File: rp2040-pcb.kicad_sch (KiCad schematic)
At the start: 43 parts, among them J1 Conn_01x20_Male, J2 Conn_01x20_Male, J3 105450-0101, SW1 SW_Push, SW2 SW_Push, U1 TPS54202DDC, U2 W25Q128JVSIQ, U3 RP2040, Y1 12 MHz

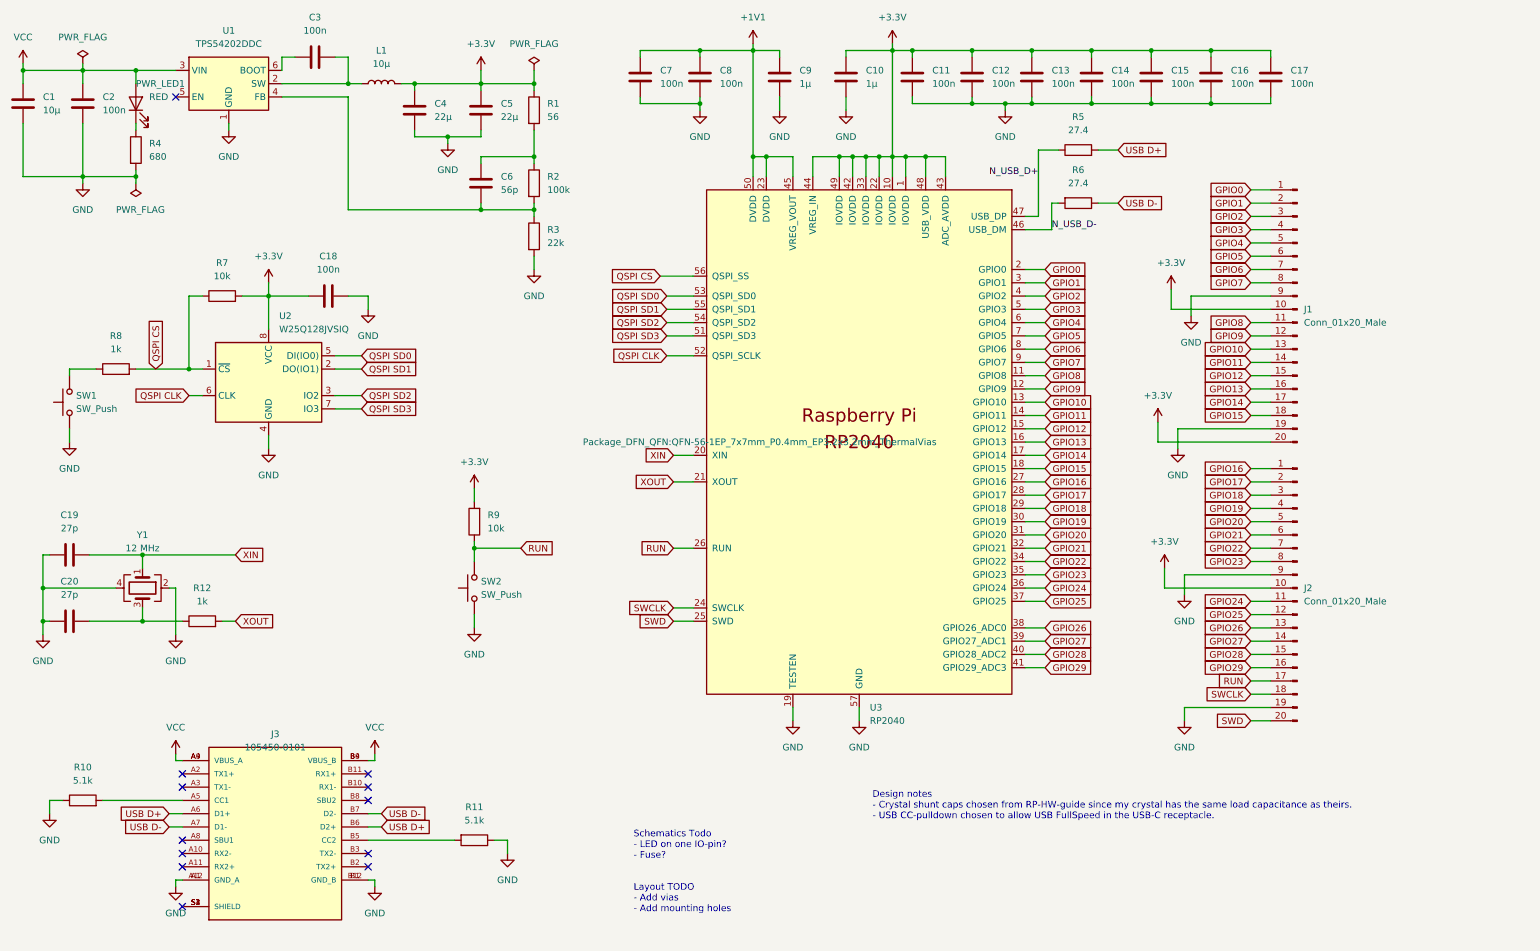
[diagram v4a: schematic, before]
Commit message: Updated numbering. Updated USB footpring on PCB.
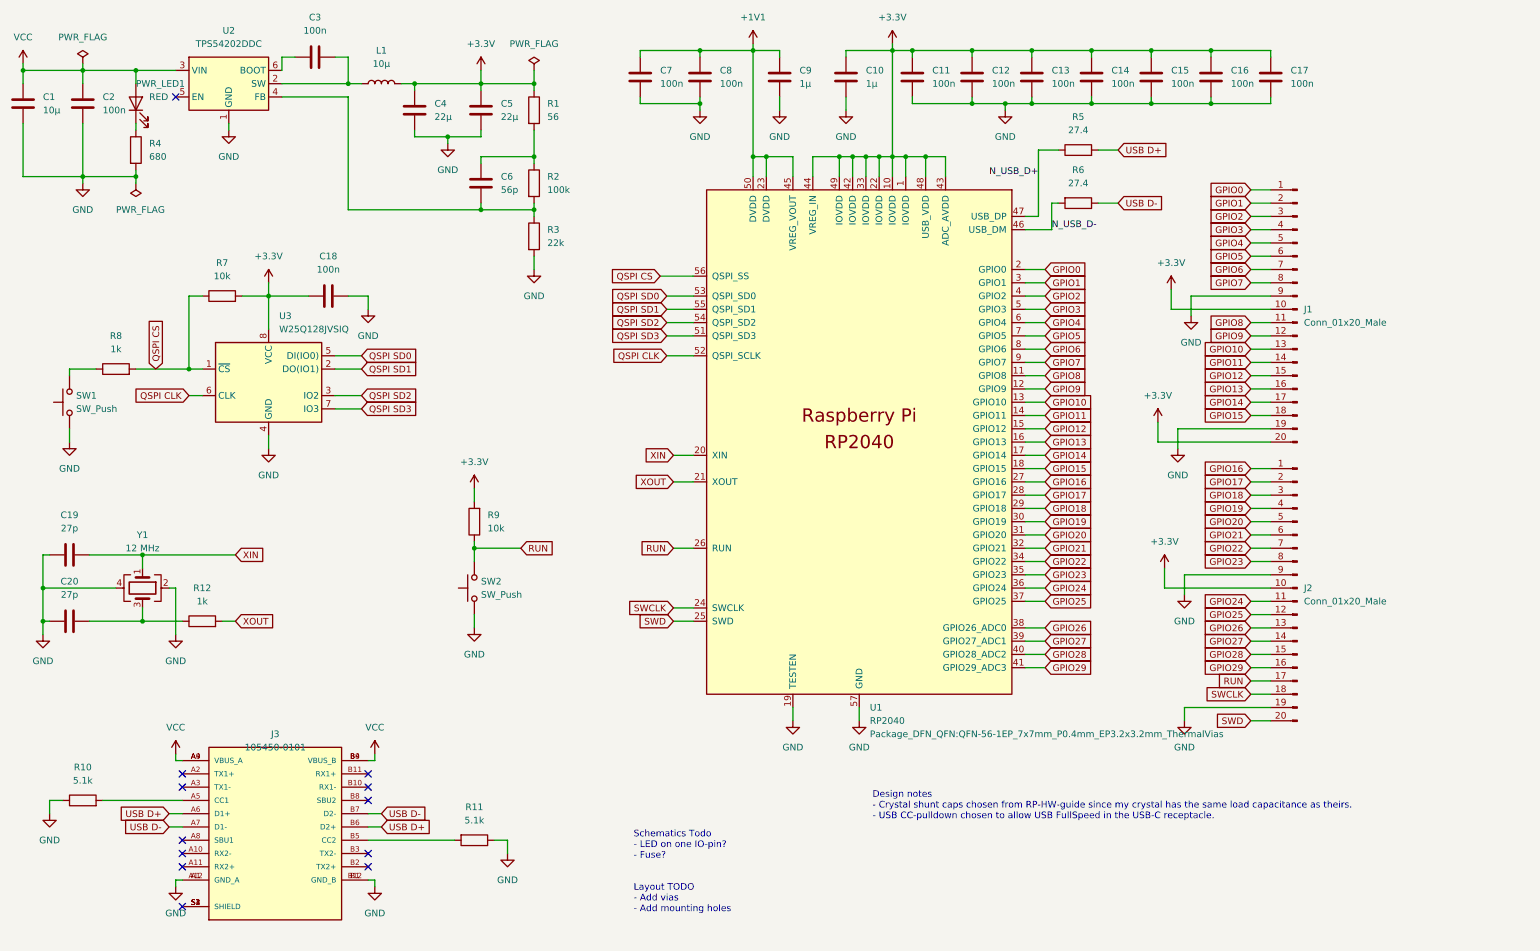
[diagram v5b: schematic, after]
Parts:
- renumbered U3 to U1, U1 to U2, U2 to U3
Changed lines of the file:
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@@
   (symbol (lib_id "MCU_RaspberryPi_RP2040:RP2040") (at 176.53 101.6 0) (unit 1)
     (in_bom yes) (on_board yes) (fields_autoplaced)
-    (property "Reference" "U3" (id 0) (at 178.5494 152.4 0)
+    (property "Reference" "U1" (id 0) (at 178.5494 152.4 0)
       (effects (font (size 1.27 1.27)) (justify left))
     )
@@
       (effects (font (size 1.27 1.27)) (justify left))
     )
-    (property "Footprint" "Package_DFN_QFN:QFN-56-1EP_7x7mm_P0.4mm_EP3.2x3.2mm_ThermalVias" (id 2) (at 157.48 101.6 0))
+    (property "Footprint" "Package_DFN_QFN:QFN-56-1EP_7x7mm_P0.4mm_EP3.2x3.2mm_ThermalVias" (id 2) (at 178.5494 157.48 0)
+      (effects (font (size 1.27 1.27)) (justify left))
+    )
     (property "Datasheet" "" (id 3) (at 157.48 101.6 0)
       (effects (font (size 1.27 1.27)) hide)
@@
   (symbol (lib_id "Memory_Flash:W25Q128JVS") (at 63.5 90.17 0) (unit 1)
     (in_bom yes) (on_board yes) (fields_autoplaced)
-    (property "Reference" "U2" (id 0) (at 65.5194 77.47 0)
+    (property "Reference" "U3" (id 0) (at 65.5194 77.47 0)
       (effects (font (size 1.27 1.27)) (justify left))
     )
@@
   (symbol (lib_id "Regulator_Switching:TPS54202DDC") (at 55.88 33.02 0) (unit 1)
     (in_bom yes) (on_board yes) (fields_autoplaced)
-    (property "Reference" "U1" (id 0) (at 55.88 22.86 0))
+    (property "Reference" "U2" (id 0) (at 55.88 22.86 0))
     (property "Value" "TPS54202DDC" (id 1) (at 55.88 25.4 0))
     (property "Footprint" "Package_TO_SOT_SMD:SOT-23-6" (id 2) (at 57.15 41.91 0)
@@
       (reference "SW2") (unit 1) (value "SW_Push") (footprint "Button_Switch_SMD:SW_SPST_TL3342")
     )
+    (path "/3ac799d5-ab17-4064-a9aa-328bd0f331fd"
+      (reference "U1") (unit 1) (value "RP2040") (footprint "Package_DFN_QFN:QFN-56-1EP_7x7mm_P0.4mm_EP3.2x3.2mm_ThermalVias")
+    )
     (path "/d079d476-6440-4c69-99b6-c646185c6bdd"
-      (reference "U1") (unit 1) (value "TPS54202DDC") (footprint "Package_TO_SOT_SMD:SOT-23-6")
+      (reference "U2") (unit 1) (value "TPS54202DDC") (footprint "Package_TO_SOT_SMD:SOT-23-6")
     )
     (path "/47447503-4624-4f7b-a2eb-ccfb50ccda8a"
-      (reference "U2") (unit 1) (value "W25Q128JVSIQ") (footprint "Package_SO:SOIC-8_5.23x5.23mm_P1.27mm")
-    )
-    (path "/3ac799d5-ab17-4064-a9aa-328bd0f331fd"
-      (reference "U3") (unit 1) (value "RP2040") (footprint "Package_DFN_QFN:QFN-56-1EP_7x7mm_P0.4mm_EP3.2x3.2mm_ThermalVias")
+      (reference "U3") (unit 1) (value "W25Q128JVSIQ") (footprint "Package_SO:SOIC-8_5.23x5.23mm_P1.27mm")
     )
     (path "/61cda4f9-deed-45ee-832d-198c2af95862"

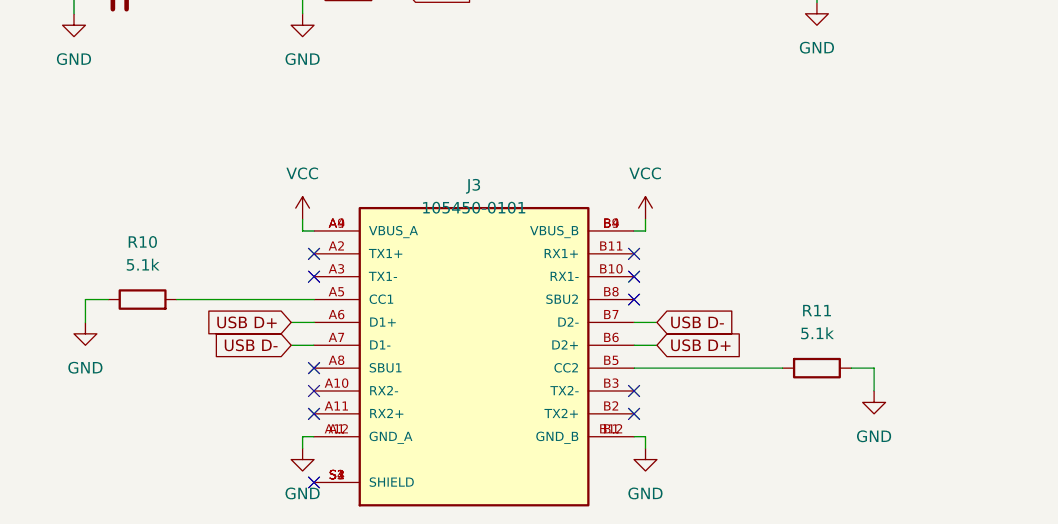
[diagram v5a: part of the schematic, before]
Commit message: Changed USB-receptacle again.
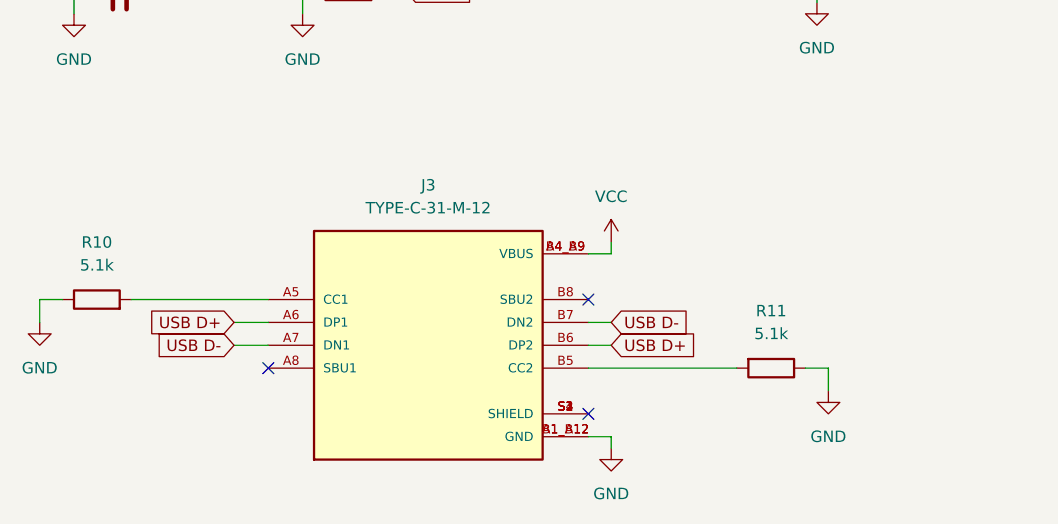
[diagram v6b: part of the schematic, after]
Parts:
- removed J3: 105450-0101, MOLEX_105450-0101, symbol 105450-0101:105450-0101
- added J3: TYPE-C-31-M-12, HRO_TYPE-C-31-M-12, symbol TYPE-C-31-M-12:TYPE-C-31-M-12
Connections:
- net GND: now also J3.A1_B12 (GND), J3.B1_A12 (GND)
- net USB D+: now also J3.A6 (DP1), J3.B6 (DP2)
- net USB D-: now also J3.A7 (DN1), J3.B7 (DN2)
- net VCC: now also J3.A4_B9 (VBUS), J3.B4_A9 (VBUS)
- net at R10.2: now also J3.A5 (CC1)
- net at R11.2: now also J3.B5 (CC2)
- new net: J3.S1 (SHIELD), J3.S2 (SHIELD), J3.S3 (SHIELD), J3.S4 (SHIELD)
- no-connect marks 12 -> 4
